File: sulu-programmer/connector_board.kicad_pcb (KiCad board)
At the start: 2 copper layers, 19.5 x 34.6 mm, 12 parts, among them J1 Conn_01x08, J2 Conn_02x04_Top_Bottom

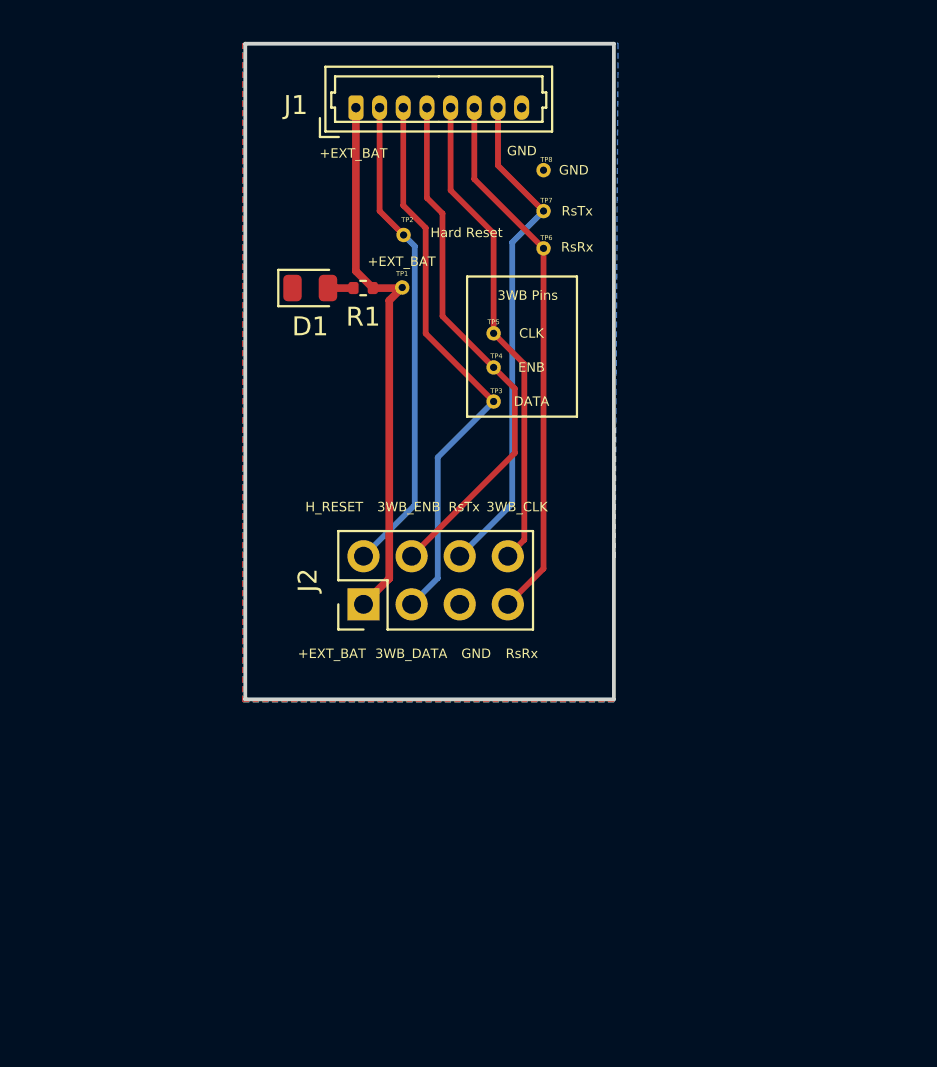
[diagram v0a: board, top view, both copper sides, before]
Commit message: Updated connector boards and Sulu-ADS1299 schematic
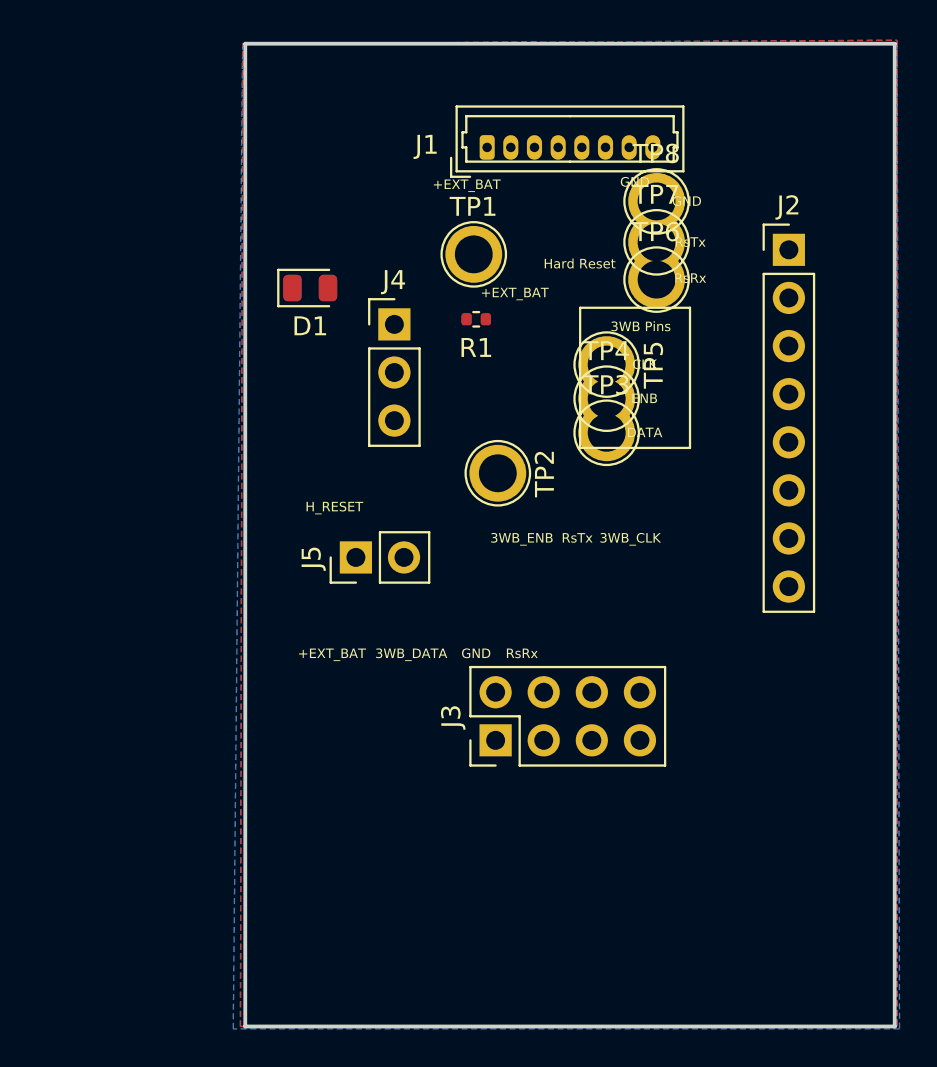
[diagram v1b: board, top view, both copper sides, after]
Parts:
- added J3: Conn_02x04_Counter_Clockwise, Connector_PinHeader_2.54mm:PinHeader_2x04_P2.54mm_Vertical, F.Cu at (93.4, 87.4)
- added J4: Conn_01x03, Connector_PinHeader_2.54mm:PinHeader_1x03_P2.54mm_Vertical, F.Cu at (88.0, 65.4)
- added J5: Conn_01x02, Connector_PinHeader_2.54mm:PinHeader_1x02_P2.54mm_Vertical, F.Cu at (86.0, 77.7)
- J2: value Conn_02x04_Top_Bottom -> Conn_01x08; footprint Connector_PinHeader_2.54mm:PinHeader_2x04_P2.54mm_Vertical -> Connector_PinHeader_2.54mm:PinHeader_1x08_P2.54mm_Vertical
- TP1, TP2, TP3, TP4, TP5, TP6, TP7, TP8: footprint SCUM:through_hole -> TestPoint:TestPoint_Plated_Hole_D2.0mm
- moved J2 29.2 mm to (108.8, 61.5), turned to 0 degrees
- moved TP2 13.5 mm to (93.5, 73.3)
- moved J1 7.24 mm to (92.9, 56.1)
- moved R1 6.19 mm to (92.3, 65.2)
- moved TP7 6.19 mm to (101.9, 61.1)
- moved TP3 6.19 mm to (99.2, 71.1)
- moved TP4 6.19 mm to (99.2, 69.3)
- moved TP5 6.19 mm to (99.2, 67.5)
- moved TP6 6.19 mm to (101.9, 63.1)
- moved TP8 6.19 mm to (101.9, 58.9)
- moved TP1 4.16 mm to (92.2, 61.7)
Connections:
- net +EXT_BAT renamed /+EXT_BAT
- J2 pad 5: GND -> /3WB_CLK
- J2 pad 6: /RsTx -> /RsRx
- J2 pad 7: /RsRx -> /RsTx
- J2 pad 8: /3WB_CLK -> GND
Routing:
- net /3WB_DATA: track 30.0 -> 0.00 mm
- net /+EXT_BAT: track 29.0 -> 0.00 mm
- net /RsRx: track 28.5 -> 0.00 mm
- net /3WB_ENB: track 27.9 -> 0.00 mm
- net /RsTx: track 26.5 -> 0.00 mm
- net /3WB_CLK: track 25.7 -> 0.00 mm
- net /HARD_RESET: track 25.6 -> 0.00 mm
- net Net-(D1-Pad2): track 1.35 -> 0.00 mm
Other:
- board size 19.5 x 34.6 mm -> 34.3 x 51.9 mm

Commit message: Sulu-ADS1299 and connector board layout+sch progress
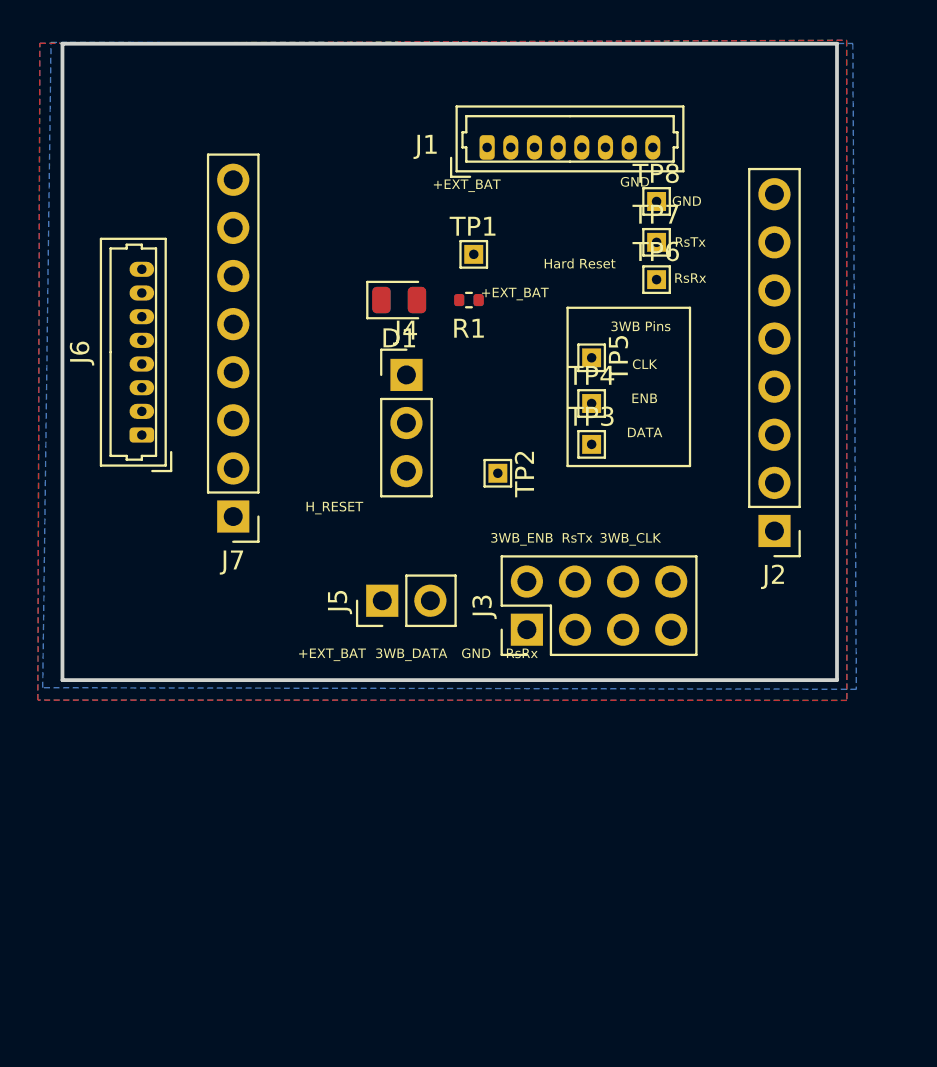
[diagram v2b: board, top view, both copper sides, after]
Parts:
- added J6: Conn_01x08, Connector_Molex:Molex_PicoBlade_53047-0810_1x08_P1.25mm_Vertical, F.Cu at (74.7, 71.3)
- added J7: Conn_01x08, Connector_PinHeader_2.54mm:PinHeader_1x08_P2.54mm_Vertical, F.Cu at (79.5, 75.6)
- TP1, TP2, TP3, TP4, TP5, TP6, TP7, TP8: footprint TestPoint:TestPoint_Plated_Hole_D2.0mm -> TestPoint:TestPoint_THTPad_1.0x1.0mm_Drill0.5mm
- moved J2 14.9 mm to (108.1, 76.3), turned to 180 degrees
- moved J3 6.07 mm to (95.0, 81.5)
- moved D1 4.74 mm to (88.3, 64.1)
- moved J4 2.74 mm to (88.6, 68.1)
- moved J5 2.68 mm to (87.4, 80.0)
- moved R1 1.09 mm to (91.9, 64.1)
- moved TP3 1.00 mm to (98.4, 71.8)
- moved TP5 0.87 mm to (98.4, 67.2)
- moved TP4 0.83 mm to (98.4, 69.6)
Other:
- board size 34.3 x 51.9 mm -> 40.9 x 33.6 mm

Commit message: SCuM Programmer Rev. 2, submitted for fab
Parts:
- added TP10: TestPoint, TestPoint:TestPoint_Keystone_5010-5014_Multipurpose, F.Cu at (73.2, 83.1)
- added TP11: TestPoint, TestPoint:TestPoint_Keystone_5010-5014_Multipurpose, F.Cu at (109.2, 53.3)
- added TP12: TestPoint, TestPoint:TestPoint_Keystone_5010-5014_Multipurpose, F.Cu at (109.2, 83.1)
- added TP9: TestPoint, TestPoint:TestPoint_Keystone_5010-5014_Multipurpose, F.Cu at (73.2, 53.3)
- R1: value 100 -> 300
- moved J4 14.3 mm to (83.8, 54.6), turned to 90 degrees
- moved TP8 12.6 mm to (89.4, 60.7)
- moved R1 5.55 mm to (90.9, 69.6), turned to 90 degrees
- moved TP7 4.84 mm to (97.0, 60.7)
- moved D1 3.60 mm to (90.9, 66.5), turned to -90 degrees
- moved TP6 2.80 mm to (100.3, 60.7)
- moved TP2 2.80 mm to (96.3, 73.2), turned to 0 degrees
- moved TP4 2.39 mm to (96.3, 68.6)
- moved TP5 2.33 mm to (96.3, 66.3)
- moved TP3 2.33 mm to (96.3, 70.9)
- moved J1 2.22 mm to (94.8, 54.9)
- moved J3 2.04 mm to (93.0, 81.5)
- moved J5 1.54 mm to (87.6, 81.5), turned to 180 degrees
- moved J7 1.37 mm to (80.3, 76.7)
- moved TP1 1.27 mm to (93.0, 60.7)
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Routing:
- net /+EXT_BAT: track 0.00 -> 52.4 mm
- net /RsTx: track 0.00 -> 44.3 mm, vias 0 -> 1
- net /3WB_DATA: track 0.00 -> 43.2 mm, vias 0 -> 1
- net /3WB_CLK: track 0.00 -> 41.8 mm, vias 0 -> 1
- net /HARD_RESET: track 0.00 -> 41.0 mm, vias 0 -> 2
- net /3WB_ENB: track 0.00 -> 39.4 mm
- net /RsRx: track 0.00 -> 36.4 mm, vias 0 -> 2
- net /+1.8V_ADS: track 0.00 -> 7.80 mm
- net /SCUM_GPIO0: track 0.00 -> 7.77 mm
- net /+1.8V_SCUM: track 0.00 -> 7.27 mm
- net /SCUM_GPIO3: track 0.00 -> 7.09 mm
- net /SCUM_GPIO14: track 0.00 -> 6.73 mm
- net /SCUM_GPIO4: track 0.00 -> 6.56 mm
- net /SCUM_GPIO13: track 0.00 -> 6.20 mm
- net /SCUM_GPIO7: track 0.00 -> 6.02 mm
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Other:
- board size 40.9 x 33.6 mm -> 41.4 x 35.1 mm
- board text added: "+1.8V_ADS"
- board text added: "+1.8V_SCUM"
- board text added: "3WB CLK"
- board text added: "3WB DATA"
- board text added: "3WB ENB"
- board text added: "BOOT"
- board text added: "Berkeley Autonomous Microsystems Lab SCuM Programmer Rev. 2"
- board text added: "DEBUG"
- board text added: "EXT BAT"
- board text added: "EXT_BAT"
- board text added: "For use with Sulu-ADS1299"
- board text added: "GPIO0"
- board text added: "GPIO13"
- board text added: "GPIO14"
- board text added: "GPIO3"
- board text added: "GPIO4"
- board text added: "GPIO7"
- board text added: "HARD RESET"
- board text added: "HRESET"
- board text added: "RS RX"
- board text added: "RSRX"
- board text added: "RSTX"
- board text added: "RX TX"
- board text removed: "3WB_CLK"
- board text removed: "3WB_DATA"
- board text removed: "3WB_ENB"
- board text removed: "CLK"
- board text removed: "DATA"
- board text removed: "ENB"
- board text removed: "H_RESET"
- board text removed: "Hard Reset"
